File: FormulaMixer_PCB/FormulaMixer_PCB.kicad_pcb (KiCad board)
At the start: 4 copper layers, 74.5 x 76.8 mm, 45 parts, among them J1 Conn_01x04, J2 Conn_01x04, J3 Conn_01x04, J4 Conn_01x04, J5 Conn_01x02, Q1 BC847, Q2 BC847, SW1 RotaryEncoder_Switch, SW2 SW_Push, SW3 SW_Push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

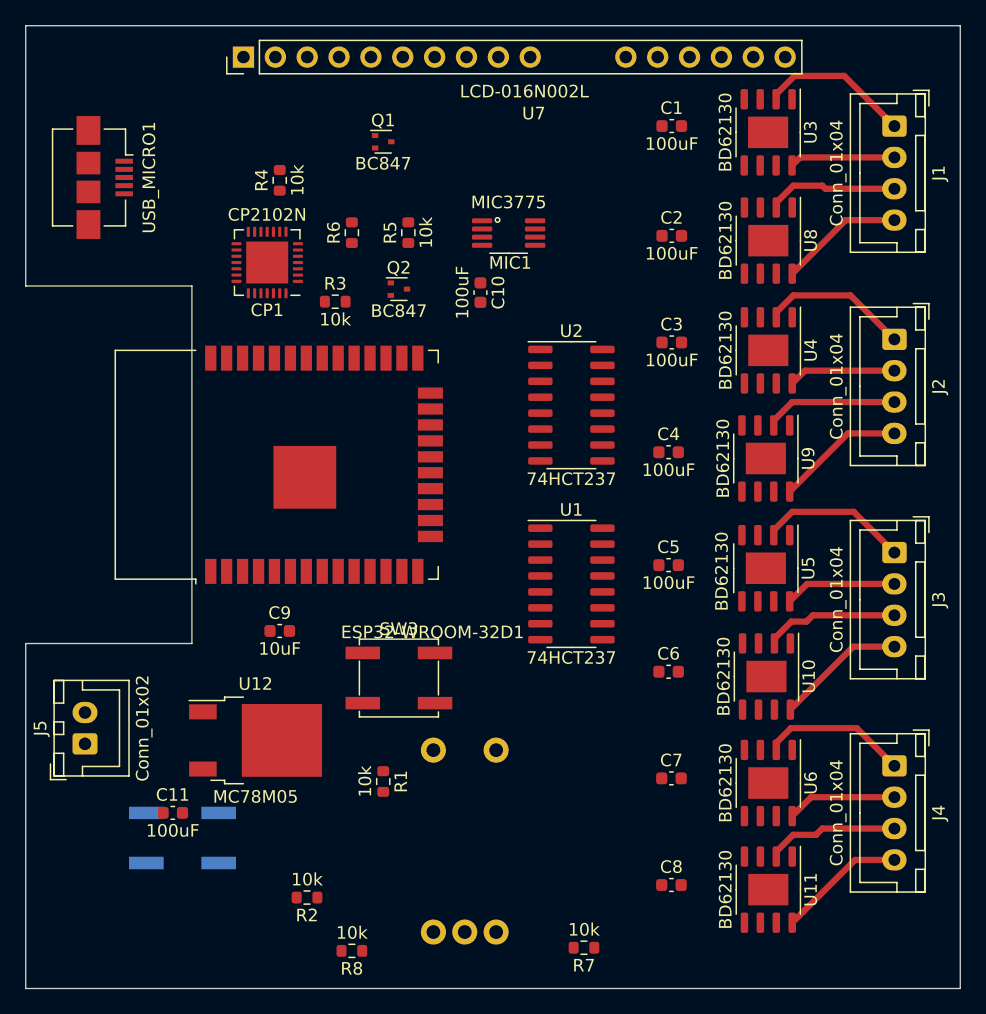
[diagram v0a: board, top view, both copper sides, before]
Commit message: Route PCB, melt PCB
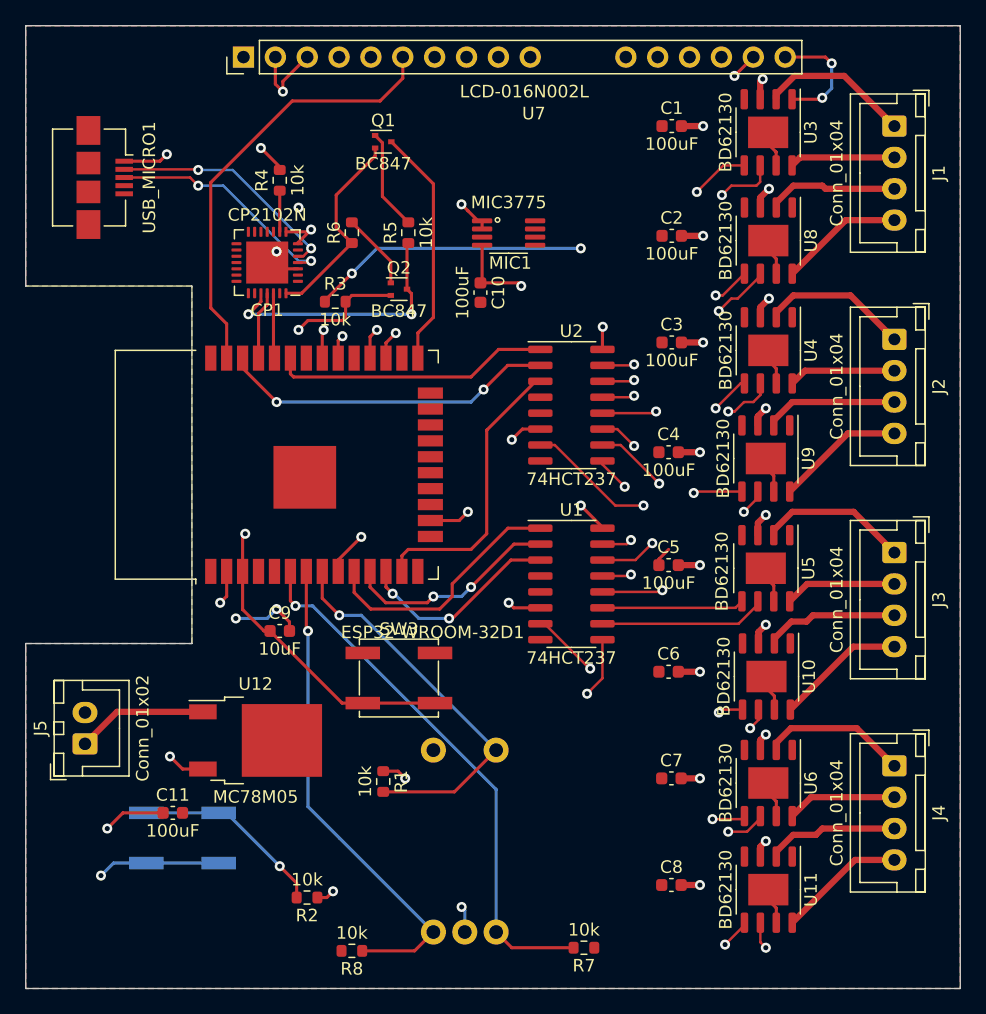
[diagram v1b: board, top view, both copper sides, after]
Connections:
- U10 pad 9: (no net) -> GND
- U11 pad 9: (no net) -> GND
- U3 pad 9: (no net) -> GND
- U4 pad 9: (no net) -> GND
- U5 pad 9: (no net) -> GND
- U6 pad 9: (no net) -> GND
- U8 pad 9: (no net) -> GND
- U9 pad 9: (no net) -> GND
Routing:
- net GND: track 0.00 -> 57.8 mm, vias 0 -> 7
- net /RESET: track 0.00 -> 51.8 mm, vias 0 -> 2
- net /P2M4_N: track 0.00 -> 51.7 mm, vias 0 -> 2
- net /BTN: track 0.00 -> 47.9 mm, vias 0 -> 2
- net /DB7: track 0.00 -> 47.9 mm, vias 0 -> 1
- net +3V3: track 0.00 -> 46.5 mm, vias 0 -> 11
- net /P2M4_P: track 0.00 -> 45.2 mm, vias 0 -> 2
- net /ENC_A: track 0.00 -> 43.0 mm, vias 0 -> 1
- net /P1M1_N: track 0.00 -> 39.4 mm, vias 0 -> 2
- net /ENC_B: track 0.00 -> 39.2 mm, vias 0 -> 1
- net /P1M1_P: track 0.00 -> 38.0 mm, vias 0 -> 2
- net +12V: track 0.00 -> 37.1 mm, vias 0 -> 16
- net /E: track 0.00 -> 35.0 mm
- net /DB6: track 0.00 -> 34.9 mm, vias 0 -> 1
- net /DB4: track 0.00 -> 34.3 mm, vias 0 -> 1
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- added copper zone on B.Cu, net +12V
- added copper zone on In1.Cu, net +3V3
- added copper zone on In2.Cu, net +5V
- added copper zone on F.Cu, net GND
